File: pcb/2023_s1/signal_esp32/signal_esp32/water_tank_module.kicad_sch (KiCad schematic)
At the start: 13 parts, among them J1 Conn_01x05_Male, J2 Conn_01x02_Male, U4 NRF24L01_Breakout

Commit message: fix, added a 4th mounting hole and rerouted the pcb in order to make feasible to solder given our poor infrastructure for PCB production
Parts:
- added H?: MountingHole, MountingHole:MountingHole_2.7mm_M2.5_Pad, symbol Mechanical:MountingHole
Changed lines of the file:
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@@
     (pin "9")
+  )
+  (symbol (lib_id "Mechanical:MountingHole") (at 39.37 73.66 0) (unit 1)
+    (in_bom yes) (on_board yes) (fields_autoplaced)
+    (property "Reference" "H?" (id 0) (at 41.91 72.3899 0)
+      (effects (font (size 1.27 1.27)) (justify left))
+    )
+    (property "Value" "MountingHole" (id 1) (at 41.91 74.9299 0)
+      (effects (font (size 1.27 1.27)) (justify left))
+    )
+    (property "Footprint" "MountingHole:MountingHole_2.7mm_M2.5_Pad" (id 2) (at 39.37 73.66 0)
+      (effects (font (size 1.27 1.27)) hide)
+    )
+    (property "Datasheet" "~" (id 3) (at 39.37 73.66 0)
+      (effects (font (size 1.27 1.27)) hide)
+    )
   )
   (symbol (lib_id "Connector:Conn_01x02_Male") (at 92.71 93.98 180) (unit 1)
@@
       (reference "H3") (unit 1) (value "MountingHole") (footprint "MountingHole:MountingHole_2.7mm_M2.5_Pad")
     )
+    (path "/d631f944-c6fd-4c1f-b6f6-5dd9ebd19282"
+      (reference "H?") (unit 1) (value "MountingHole") (footprint "MountingHole:MountingHole_2.7mm_M2.5_Pad")
+    )
     (path "/0acd31bd-0a92-415d-b1ae-b860cc8ad816"

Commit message: fix, added a 4th mounting hole
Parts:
- gave numbers to parts that had none: 1
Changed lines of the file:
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@@
   (symbol (lib_id "Mechanical:MountingHole") (at 39.37 73.66 0) (unit 1)
     (in_bom yes) (on_board yes) (fields_autoplaced)
-    (property "Reference" "H?" (id 0) (at 41.91 72.3899 0)
+    (property "Reference" "H4" (id 0) (at 41.91 72.3899 0)
       (effects (font (size 1.27 1.27)) (justify left))
     )
@@
     )
     (path "/d631f944-c6fd-4c1f-b6f6-5dd9ebd19282"
-      (reference "H?") (unit 1) (value "MountingHole") (footprint "MountingHole:MountingHole_2.7mm_M2.5_Pad")
+      (reference "H4") (unit 1) (value "MountingHole") (footprint "MountingHole:MountingHole_2.7mm_M2.5_Pad")
     )
     (path "/0acd31bd-0a92-415d-b1ae-b860cc8ad816"

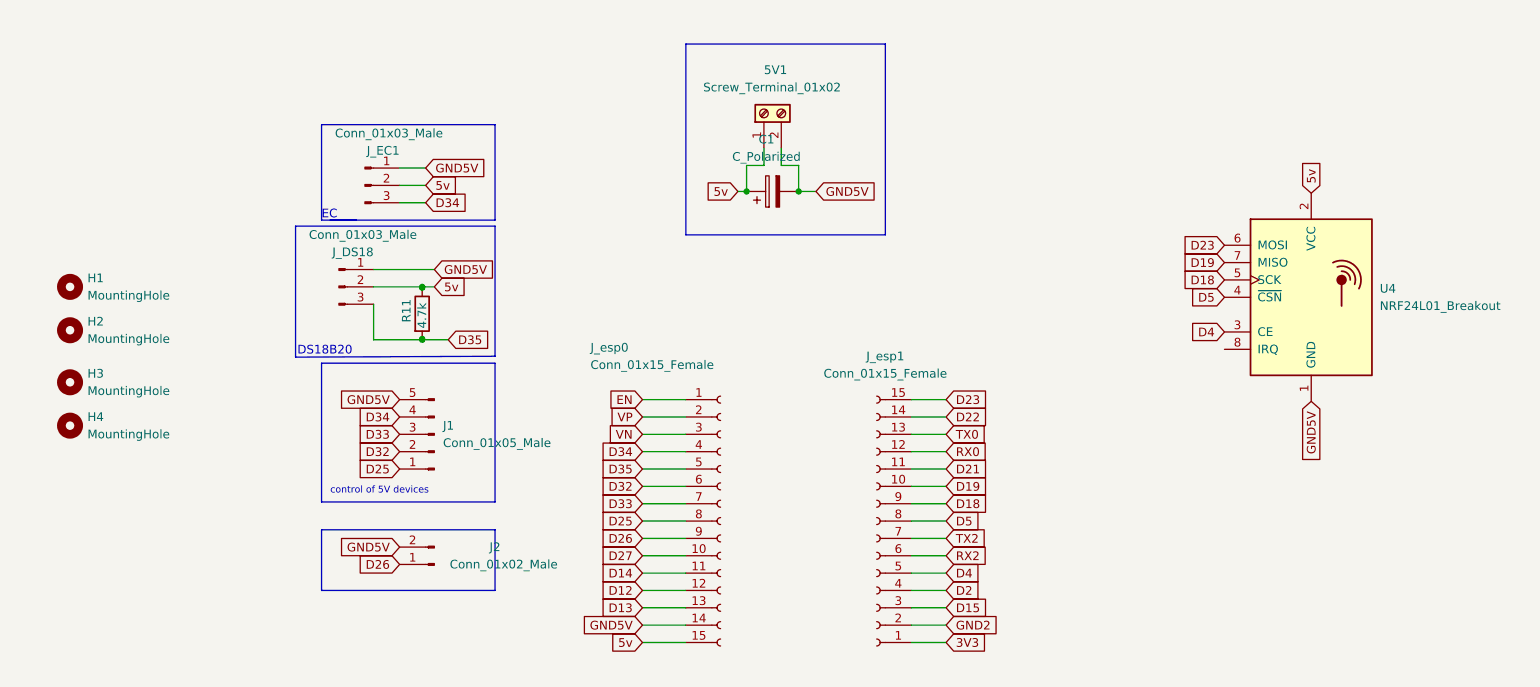
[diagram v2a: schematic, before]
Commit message: update, reselection of output pins and ds18b20 pin, rerouting and resizing of pads
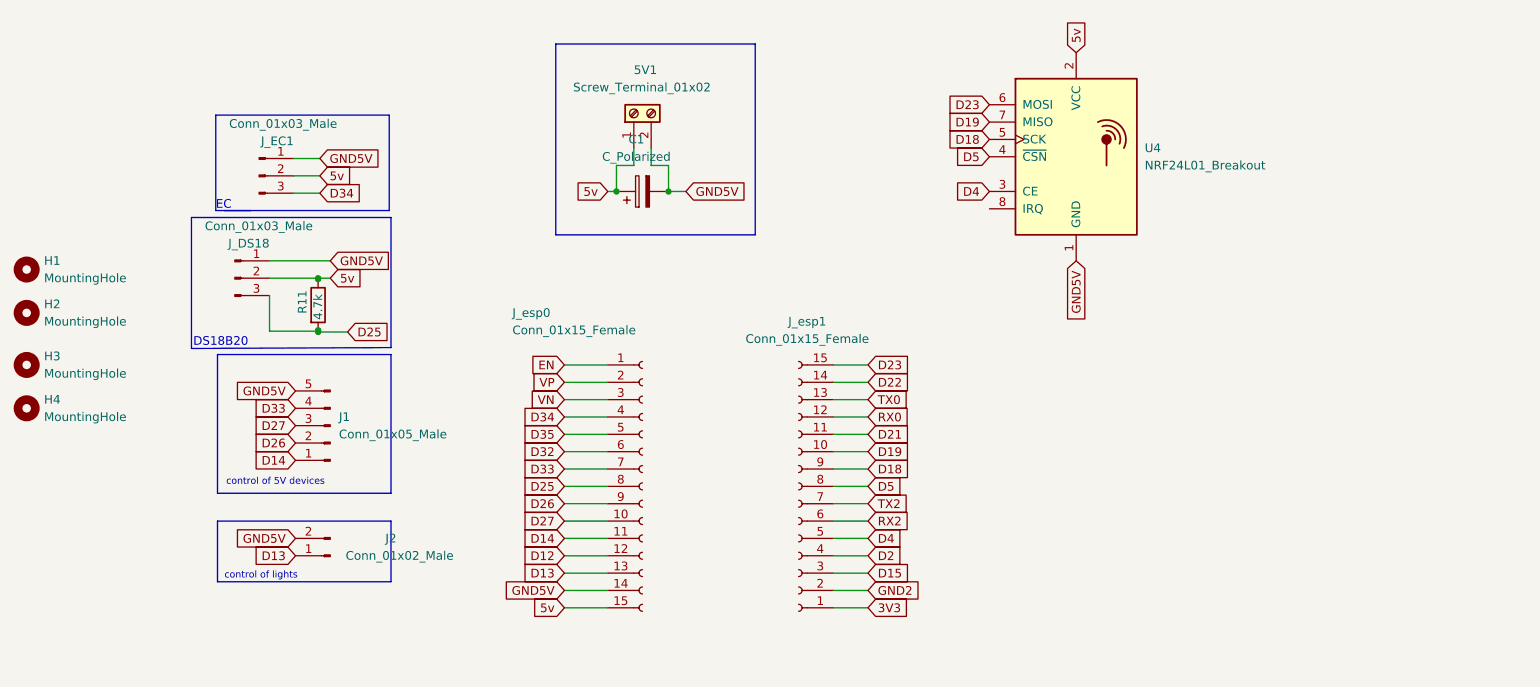
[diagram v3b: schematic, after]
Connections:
- net D13: now also J2.1 (Pin_1)
- net D14: now also J1.1 (Pin_1)
- net D25: now also J_DS18.3 (Pin_3), R11.2; no longer J1.1 (Pin_1)
- net D26: now also J1.2 (Pin_2); no longer J2.1 (Pin_1)
- net D27: now also J1.3 (Pin_3)
- net D32: no longer J1.2 (Pin_2)
- net D33: now also J1.4 (Pin_4); no longer J1.3 (Pin_3)
- net D34: no longer J1.4 (Pin_4)
- net D35: no longer J_DS18.3 (Pin_3), R11.2
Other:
- note added: "control of lights"
- moved on the sheet: 5V1, C1, H1, H2, H3, H4, J1, J2, J_DS18, J_EC1, J_esp0, J_esp1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

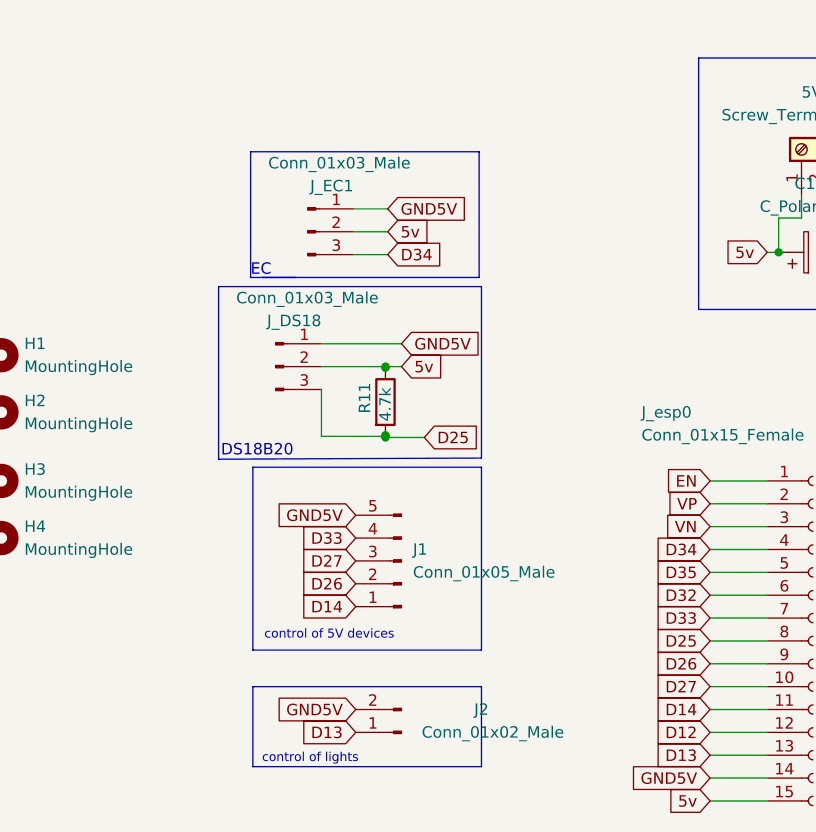
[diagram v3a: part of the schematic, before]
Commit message: update, changed some terminals to screw terminals for easyer connection
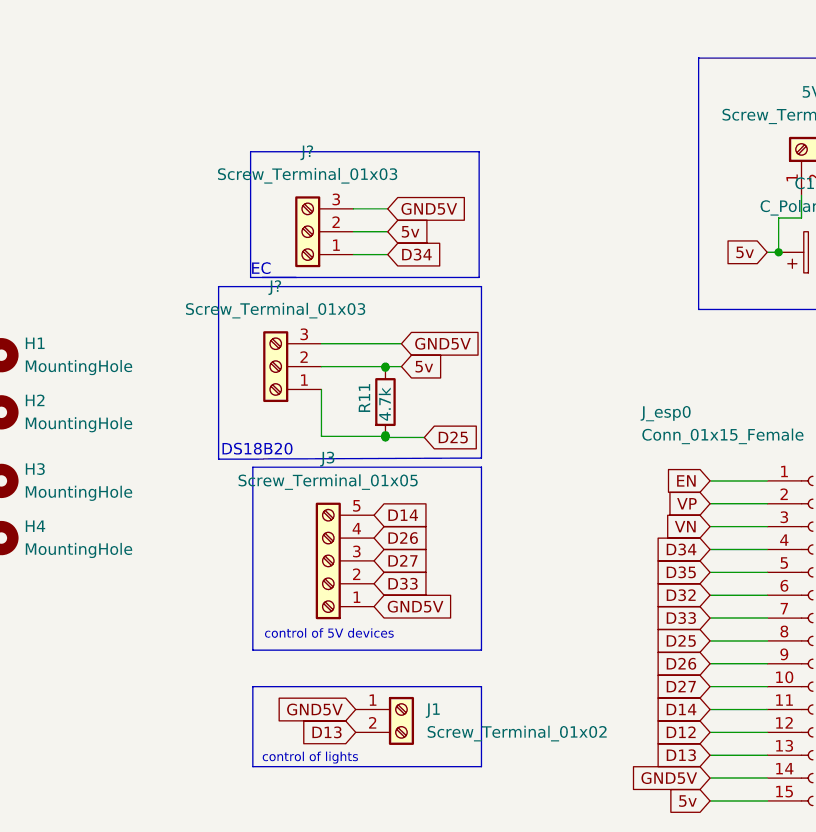
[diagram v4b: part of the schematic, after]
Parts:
- removed J1: Conn_01x05_Male, Connector_JST:JST_EH_B5B-EH-A_1x05_P2.50mm_Vertical, symbol Connector:Conn_01x05_Male
- removed J2: Conn_01x02_Male, Connector_JST:JST_EH_B2B-EH-A_1x02_P2.50mm_Vertical, symbol Connector:Conn_01x02_Male
- removed J_DS18, J_EC1: Conn_01x03_Male, Connector_JST:JST_EH_B3B-EH-A_1x03_P2.50mm_Vertical, symbol Connector:Conn_01x03_Male
- added J1: Screw_Terminal_01x02, symbol Connector:Screw_Terminal_01x02
- added J3: Screw_Terminal_01x05, TerminalBlock_Altech:Altech_AK300_1x05_P5.00mm_45-Degree, symbol Connector:Screw_Terminal_01x05
- added J?: Screw_Terminal_01x03, symbol Connector:Screw_Terminal_01x03
- added J?: Screw_Terminal_01x03, TerminalBlock_Altech:Altech_AK300_1x03_P5.00mm_45-Degree, symbol Connector:Screw_Terminal_01x03
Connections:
- net 5v: now also J?.2 (Pin_2), J?.2 (Pin_2)
- net D13: now also J1.2 (Pin_2)
- net D14: now also J3.5 (Pin_5)
- net D25: now also J?.1 (Pin_1)
- net D26: now also J3.4 (Pin_4)
- net D27: now also J3.3 (Pin_3)
- net D33: now also J3.2 (Pin_2)
- net D34: now also J?.1 (Pin_1)
- net GND5V: now also J1.1 (Pin_1), J3.1 (Pin_1), J?.3 (Pin_3), J?.3 (Pin_3)
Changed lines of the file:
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@@
     )
   )
-  (global_label "GND5V" (shape input) (at 72.39 68.58 180) (fields_autoplaced)
-    (effects (font (size 1.27 1.27)) (justify right))
-    (property "Intersheet References" "${INTERSHEET_REFS}" (id 0) (at 63.8083 68.6594 0)
-      (effects (font (size 1.27 1.27)) (justify right) hide)
+  (global_label "GND5V" (shape input) (at 74.422 78.74 0) (fields_autoplaced)
+    (effects (font (size 1.27 1.27)) (justify left))
+    (property "Intersheet References" "${INTERSHEET_REFS}" (id 0) (at 83.0037 78.6606 0)
+      (effects (font (size 1.27 1.27)) (justify left) hide)
     )
   )
@@
     )
   )
-  (global_label "D26" (shape input) (at 72.39 76.2 180) (fields_autoplaced)
-    (effects (font (size 1.27 1.27)) (justify right))
-    (property "Intersheet References" "${INTERSHEET_REFS}" (id 0) (at 66.2879 76.1206 0)
-      (effects (font (size 1.27 1.27)) (justify right) hide)
+  (global_label "D26" (shape input) (at 74.422 71.12 0) (fields_autoplaced)
+    (effects (font (size 1.27 1.27)) (justify left))
+    (property "Intersheet References" "${INTERSHEET_REFS}" (id 0) (at 80.5241 71.1994 0)
+      (effects (font (size 1.27 1.27)) (justify left) hide)
     )
   )
@@
     )
   )
-  (global_label "D33" (shape input) (at 72.39 71.12 180) (fields_autoplaced)
-    (effects (font (size 1.27 1.27)) (justify right))
-    (property "Intersheet References" "${INTERSHEET_REFS}" (id 0) (at 66.2879 71.1994 0)
-      (effects (font (size 1.27 1.27)) (justify right) hide)
+  (global_label "D33" (shape input) (at 74.422 76.2 0) (fields_autoplaced)
+    (effects (font (size 1.27 1.27)) (justify left))
+    (property "Intersheet References" "${INTERSHEET_REFS}" (id 0) (at 80.5241 76.1206 0)
+      (effects (font (size 1.27 1.27)) (justify left) hide)
     )
   )
@@
     )
   )
-  (global_label "D14" (shape input) (at 72.39 78.74 180) (fields_autoplaced)
-    (effects (font (size 1.27 1.27)) (justify right))
-    (property "Intersheet References" "${INTERSHEET_REFS}" (id 0) (at 66.2879 78.6606 0)
-      (effects (font (size 1.27 1.27)) (justify right) hide)
+  (global_label "D14" (shape input) (at 74.422 68.58 0) (fields_autoplaced)
+    (effects (font (size 1.27 1.27)) (justify left))
+    (property "Intersheet References" "${INTERSHEET_REFS}" (id 0) (at 80.5241 68.6594 0)
+      (effects (font (size 1.27 1.27)) (justify left) hide)
     )
   )
@@
     )
   )
-  (global_label "D27" (shape input) (at 72.39 73.66 180) (fields_autoplaced)
-    (effects (font (size 1.27 1.27)) (justify right))
-    (property "Intersheet References" "${INTERSHEET_REFS}" (id 0) (at 66.2879 73.5806 0)
-      (effects (font (size 1.27 1.27)) (justify right) hide)
+  (global_label "D27" (shape input) (at 74.422 73.66 0) (fields_autoplaced)
+    (effects (font (size 1.27 1.27)) (justify left))
+    (property "Intersheet References" "${INTERSHEET_REFS}" (id 0) (at 80.5241 73.7394 0)
+      (effects (font (size 1.27 1.27)) (justify left) hide)
     )
   )
@@
     )
   )
-  (symbol (lib_id "Connector:Conn_01x05_Male") (at 77.47 73.66 180) (unit 1)
-    (in_bom yes) (on_board yes) (fields_autoplaced)
-    (property "Reference" "J1" (id 0) (at 78.74 72.3899 0)
-      (effects (font (size 1.27 1.27)) (justify right))
-    )
-    (property "Value" "Conn_01x05_Male" (id 1) (at 78.74 74.9299 0)
-      (effects (font (size 1.27 1.27)) (justify right))
-    )
-    (property "Footprint" "Connector_JST:JST_EH_B5B-EH-A_1x05_P2.50mm_Vertical" (id 2) (at 77.47 73.66 0)
-      (effects (font (size 1.27 1.27)) hide)
-    )
-    (property "Datasheet" "~" (id 3) (at 77.47 73.66 0)
-      (effects (font (size 1.27 1.27)) hide)
-    )
-    (pin "1")
-    (pin "2")
-    (pin "3")
-    (pin "4")
-    (pin "5")
-  )
-  (symbol (lib_id "Connector:Conn_01x03_Male") (at 67.056 37.084 0) (unit 1)
-    (in_bom yes) (on_board yes)
-    (property "Reference" "J_EC1" (id 0) (at 72.136 32.004 0)
-      (effects (font (size 1.27 1.27)) (justify right))
-    )
-    (property "Value" "Conn_01x03_Male" (id 1) (at 78.486 29.464 0)
-      (effects (font (size 1.27 1.27)) (justify right))
-    )
-    (property "Footprint" "Connector_JST:JST_EH_B3B-EH-A_1x03_P2.50mm_Vertical" (id 2) (at 67.056 37.084 0)
-      (effects (font (size 1.27 1.27)) hide)
-    )
-    (property "Datasheet" "~" (id 3) (at 67.056 37.084 0)
-      (effects (font (size 1.27 1.27)) hide)
-    )
-    (pin "1")
-    (pin "2")
-    (pin "3")
+  (symbol (lib_id "Connector:Screw_Terminal_01x02") (at 77.47 90.17 0) (unit 1)
+    (in_bom yes) (on_board yes) (fields_autoplaced)
+    (property "Reference" "J1" (id 0) (at 80.264 90.1699 0)
+      (effects (font (size 1.27 1.27)) (justify left))
+    )
+    (property "Value" "Screw_Terminal_01x02" (id 1) (at 80.264 92.7099 0)
+      (effects (font (size 1.27 1.27)) (justify left))
+    )
+    (property "Footprint" "" (id 2) (at 77.47 90.17 0)
+      (effects (font (size 1.27 1.27)) hide)
+    )
+    (property "Datasheet" "~" (id 3) (at 77.47 90.17 0)
+      (effects (font (size 1.27 1.27)) hide)
+    )
+    (pin "1")
+    (pin "2")
   )
   (symbol (lib_id "Connector:Conn_01x15_Female") (at 123.19 82.55 0) (unit 1)
@@
     (pin "9")
   )
+  (symbol (lib_id "Connector:Screw_Terminal_01x03") (at 67.056 37.084 180) (unit 1)
+    (in_bom yes) (on_board yes) (fields_autoplaced)
+    (property "Reference" "J?" (id 0) (at 67.056 28.194 0))
+    (property "Value" "Screw_Terminal_01x03" (id 1) (at 67.056 30.734 0))
+    (property "Footprint" "" (id 2) (at 67.056 37.084 0)
+      (effects (font (size 1.27 1.27)) hide)
+    )
+    (property "Datasheet" "~" (id 3) (at 67.056 37.084 0)
+      (effects (font (size 1.27 1.27)) hide)
+    )
+    (pin "1")
+    (pin "2")
+    (pin "3")
+  )
   (symbol (lib_id "RF:NRF24L01_Breakout") (at 186.69 34.29 0) (unit 1)
     (in_bom yes) (on_board yes) (fields_autoplaced)
@@
     (pin "2")
   )
-  (symbol (lib_id "Connector:Conn_01x03_Male") (at 63.5 52.07 0) (unit 1)
-    (in_bom yes) (on_board yes)
-    (property "Reference" "J_DS18" (id 0) (at 68.58 46.99 0)
-      (effects (font (size 1.27 1.27)) (justify right))
-    )
-    (property "Value" "Conn_01x03_Male" (id 1) (at 74.93 44.45 0)
-      (effects (font (size 1.27 1.27)) (justify right))
-    )
-    (property "Footprint" "Connector_JST:JST_EH_B3B-EH-A_1x03_P2.50mm_Vertical" (id 2) (at 63.5 52.07 0)
+  (symbol (lib_id "Connector:Screw_Terminal_01x03") (at 63.5 52.07 180) (unit 1)
+    (in_bom yes) (on_board yes) (fields_autoplaced)
+    (property "Reference" "J?" (id 0) (at 63.5 43.18 0))
+    (property "Value" "Screw_Terminal_01x03" (id 1) (at 63.5 45.72 0))
+    (property "Footprint" "TerminalBlock_Altech:Altech_AK300_1x03_P5.00mm_45-Degree" (id 2) (at 63.5 52.07 0)
       (effects (font (size 1.27 1.27)) hide)
     )
@@
     (pin "2")
     (pin "3")
+  )
+  (symbol (lib_id "Connector:Screw_Terminal_01x05") (at 69.342 73.66 180) (unit 1)
+    (in_bom yes) (on_board yes) (fields_autoplaced)
+    (property "Reference" "J3" (id 0) (at 69.342 62.23 0))
+    (property "Value" "Screw_Terminal_01x05" (id 1) (at 69.342 64.77 0))
+    (property "Footprint" "TerminalBlock_Altech:Altech_AK300_1x05_P5.00mm_45-Degree" (id 2) (at 69.342 73.66 0)
+      (effects (font (size 1.27 1.27)) hide)
+    )
+    (property "Datasheet" "~" (id 3) (at 69.342 73.66 0)
+      (effects (font (size 1.27 1.27)) hide)
+    )
+    (pin "1")
+    (pin "2")
+    (pin "3")
+    (pin "4")
+    (pin "5")
   )
   (symbol (lib_id "Mechanical:MountingHole") (at 33.02 57.15 0) (unit 1)
@@
     )
   )
-  (symbol (lib_id "Connector:Conn_01x02_Male") (at 77.47 92.71 180) (unit 1)
-    (in_bom yes) (on_board yes)
-    (property "Reference" "J2" (id 0) (at 86.36 90.17 0))
-    (property "Value" "Conn_01x02_Male" (id 1) (at 87.63 92.71 0))
-    (property "Footprint" "Connector_JST:JST_EH_B2B-EH-A_1x02_P2.50mm_Vertical" (id 2) (at 77.47 92.71 0)
-      (effects (font (size 1.27 1.27)) hide)
-    )
-    (property "Datasheet" "~" (id 3) (at 77.47 92.71 0)
-      (effects (font (size 1.27 1.27)) hide)
-    )
-    (pin "1")
-    (pin "2")
-  )
   (symbol (lib_id "Mechanical:MountingHole") (at 33.02 64.77 0) (unit 1)
     (in_bom yes) (on_board yes) (fields_autoplaced)
@@
       (reference "H4") (unit 1) (value "MountingHole") (footprint "MountingHole:MountingHole_2.7mm_M2.5_Pad")
     )
-    (path "/0acd31bd-0a92-415d-b1ae-b860cc8ad816"
-      (reference "J1") (unit 1) (value "Conn_01x05_Male") (footprint "Connector_JST:JST_EH_B5B-EH-A_1x05_P2.50mm_Vertical")
-    )
-    (path "/e9985b2b-95c9-4d1b-aa33-6bba12cffcb1"
-      (reference "J2") (unit 1) (value "Conn_01x02_Male") (footprint "Connector_JST:JST_EH_B2B-EH-A_1x02_P2.50mm_Vertical")
-    )
-    (path "/977a8c43-25e0-4675-a166-3f6d7cf1e985"
-      (reference "J_DS18") (unit 1) (value "Conn_01x03_Male") (footprint "Connector_JST:JST_EH_B3B-EH-A_1x03_P2.50mm_Vertical")
-    )
-    (path "/14d2c33f-db1c-4934-9099-a11479410209"
-      (reference "J_EC1") (unit 1) (value "Conn_01x03_Male") (footprint "Connector_JST:JST_EH_B3B-EH-A_1x03_P2.50mm_Vertical")
+    (path "/3adfe60e-0080-40d8-9c73-678f3a41ec6a"
+      (reference "J1") (unit 1) (value "Screw_Terminal_01x02") (footprint "TerminalBlock_Altech:Altech_AK300_1x02_P5.00mm_45-Degree")
+    )
+    (path "/83870249-aa7f-4c7c-8f54-f29bd8752375"
+      (reference "J3") (unit 1) (value "Screw_Terminal_01x05") (footprint "TerminalBlock_Altech:Altech_AK300_1x05_P5.00mm_45-Degree")
+    )
+    (path "/7468bafd-354a-4266-b175-876eeab66a22"
+      (reference "J?") (unit 1) (value "Screw_Terminal_01x03") (footprint "TerminalBlock_Altech:Altech_AK300_1x03_P5.00mm_45-Degree")
+    )
+    (path "/82cde8f6-0e2e-4e52-8989-64d7f41077bd"
+      (reference "J?") (unit 1) (value "Screw_Terminal_01x03") (footprint "TerminalBlock_Altech:Altech_AK300_1x03_P5.00mm_45-Degree")
     )
     (path "/46174da3-e018-4f2d-abee-13fae04c49fe"

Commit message: update
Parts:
- J1: footprint (none) -> TerminalBlock_Altech:Altech_AK300_1x02_P5.00mm_45-Degree
- J?: footprint (none) -> TerminalBlock_Altech:Altech_AK300_1x03_P5.00mm_45-Degree
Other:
- moved on the sheet: J1, J3, J?, R11
